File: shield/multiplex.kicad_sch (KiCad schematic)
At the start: 2 parts

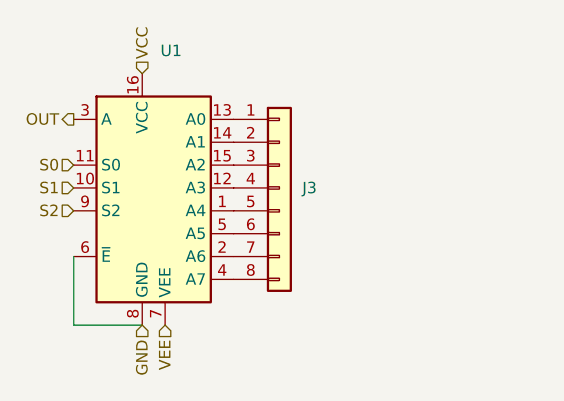
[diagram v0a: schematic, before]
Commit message: Move incomplete shield to separate dir, and add complete breakout design for a single multiplexer.
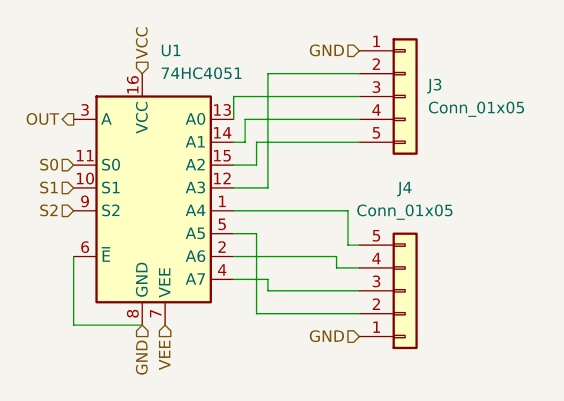
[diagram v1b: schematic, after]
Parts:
- removed J3: (no value), Connector_PinHeader_2.54mm:PinHeader_1x08_P2.54mm_Vertical, symbol Connector_Generic:Conn_01x08
- added J3, J4: Conn_01x05, Connector_PinHeader_2.54mm:PinHeader_1x05_P2.54mm_Vertical, symbol Connector_Generic:Conn_01x05
- U1: value (none) -> 74HC4051
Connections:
- net GND: now also J3.1 (Pin_1), J4.1 (Pin_1)
- net at U1.1 (A4): now also J4.5 (Pin_5)
- net at U1.12 (A3): now also J3.2 (Pin_2)
- net at U1.13 (A0): now also J3.3 (Pin_3)
- net at U1.14 (A1): now also J3.4 (Pin_4)
- net at U1.15 (A2): now also J3.5 (Pin_5)
- net at U1.2 (A6): now also J4.4 (Pin_4)
- net at U1.4 (A7): now also J4.3 (Pin_3)
- net at U1.5 (A5): now also J4.2 (Pin_2)
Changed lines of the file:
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@@
 (kicad_sch (version 20211123) (generator eeschema)
   (paper "A4")
+  (wire (pts (xy 104.14 49.53) (xy 104.14 62.23))
+    (stroke (width 0) (type default) (color 0 0 0 0))
+  )
+  (wire (pts (xy 100.33 72.39) (xy 104.14 72.39))
+    (stroke (width 0) (type default) (color 0 0 0 0))
+  )
   (wire (pts (xy 82.55 77.47) (xy 90.17 77.47))
     (stroke (width 0) (type default) (color 0 0 0 0))
   )
+  (wire (pts (xy 101.6 54.61) (xy 114.3 54.61))
+    (stroke (width 0) (type default) (color 0 0 0 0))
+  )
+  (wire (pts (xy 101.6 57.15) (xy 101.6 54.61))
+    (stroke (width 0) (type default) (color 0 0 0 0))
+  )
+  (wire (pts (xy 104.14 49.53) (xy 114.3 49.53))
+    (stroke (width 0) (type default) (color 0 0 0 0))
+  )
+  (wire (pts (xy 100.33 62.23) (xy 104.14 62.23))
+    (stroke (width 0) (type default) (color 0 0 0 0))
+  )
+  (wire (pts (xy 100.33 64.77) (xy 113.03 64.77))
+    (stroke (width 0) (type default) (color 0 0 0 0))
+  )
+  (wire (pts (xy 100.33 69.85) (xy 111.76 69.85))
+    (stroke (width 0) (type default) (color 0 0 0 0))
+  )
+  (wire (pts (xy 111.76 71.12) (xy 114.3 71.12))
+    (stroke (width 0) (type default) (color 0 0 0 0))
+  )
+  (wire (pts (xy 102.87 59.69) (xy 102.87 57.15))
+    (stroke (width 0) (type default) (color 0 0 0 0))
+  )
+  (wire (pts (xy 104.14 72.39) (xy 104.14 73.66))
+    (stroke (width 0) (type default) (color 0 0 0 0))
+  )
+  (wire (pts (xy 100.33 54.61) (xy 100.33 52.07))
+    (stroke (width 0) (type default) (color 0 0 0 0))
+  )
+  (wire (pts (xy 111.76 69.85) (xy 111.76 71.12))
+    (stroke (width 0) (type default) (color 0 0 0 0))
+  )
+  (wire (pts (xy 100.33 59.69) (xy 102.87 59.69))
+    (stroke (width 0) (type default) (color 0 0 0 0))
+  )
+  (wire (pts (xy 113.03 68.58) (xy 114.3 68.58))
+    (stroke (width 0) (type default) (color 0 0 0 0))
+  )
+  (wire (pts (xy 102.87 76.2) (xy 114.3 76.2))
+    (stroke (width 0) (type default) (color 0 0 0 0))
+  )
+  (wire (pts (xy 100.33 67.31) (xy 102.87 67.31))
+    (stroke (width 0) (type default) (color 0 0 0 0))
+  )
+  (wire (pts (xy 102.87 67.31) (xy 102.87 76.2))
+    (stroke (width 0) (type default) (color 0 0 0 0))
+  )
+  (wire (pts (xy 113.03 64.77) (xy 113.03 68.58))
+    (stroke (width 0) (type default) (color 0 0 0 0))
+  )
+  (wire (pts (xy 100.33 52.07) (xy 114.3 52.07))
+    (stroke (width 0) (type default) (color 0 0 0 0))
+  )
+  (wire (pts (xy 102.87 57.15) (xy 114.3 57.15))
+    (stroke (width 0) (type default) (color 0 0 0 0))
+  )
   (wire (pts (xy 82.55 69.85) (xy 82.55 77.47))
+    (stroke (width 0) (type default) (color 0 0 0 0))
+  )
+  (wire (pts (xy 104.14 73.66) (xy 114.3 73.66))
+    (stroke (width 0) (type default) (color 0 0 0 0))
+  )
+  (wire (pts (xy 100.33 57.15) (xy 101.6 57.15))
     (stroke (width 0) (type default) (color 0 0 0 0))
   )
@@
     (effects (font (size 1.27 1.27)) (justify left))
   )
+  (hierarchical_label "GND" (shape input) (at 114.3 46.99 180)
+    (effects (font (size 1.27 1.27)) (justify right))
+  )
   (hierarchical_label "GND" (shape input) (at 90.17 77.47 270)
+    (effects (font (size 1.27 1.27)) (justify right))
+  )
+  (hierarchical_label "GND" (shape input) (at 114.3 78.74 180)
     (effects (font (size 1.27 1.27)) (justify right))
   )
@@
     (effects (font (size 1.27 1.27)) (justify right))
   )
+  (symbol (lib_id "Connector_Generic:Conn_01x05") (at 119.38 52.07 0) (unit 1)
+    (in_bom yes) (on_board yes) (fields_autoplaced)
+    (property "Reference" "J3" (id 0) (at 121.92 50.7999 0)
+      (effects (font (size 1.27 1.27)) (justify left))
+    )
+    (property "Value" "Conn_01x05" (id 1) (at 121.92 53.3399 0)
+      (effects (font (size 1.27 1.27)) (justify left))
+    )
+    (property "Footprint" "Connector_PinHeader_2.54mm:PinHeader_1x05_P2.54mm_Vertical" (id 2) (at 119.38 52.07 0)
+      (effects (font (size 1.27 1.27)) hide)
+    )
+    (property "Datasheet" "~" (id 3) (at 119.38 52.07 0)
+      (effects (font (size 1.27 1.27)) hide)
+    )
+    (pin "1")
+    (pin "2")
+    (pin "3")
+    (pin "4")
+    (pin "5")
+  )
+  (symbol (lib_id "Connector_Generic:Conn_01x05") (at 119.38 73.66 0) (mirror x) (unit 1)
+    (in_bom yes) (on_board yes) (fields_autoplaced)
+    (property "Reference" "J4" (id 0) (at 119.38 62.23 0))
+    (property "Value" "Conn_01x05" (id 1) (at 119.38 64.77 0))
+    (property "Footprint" "Connector_PinHeader_2.54mm:PinHeader_1x05_P2.54mm_Vertical" (id 2) (at 119.38 73.66 0)
+      (effects (font (size 1.27 1.27)) hide)
+    )
+    (property "Datasheet" "~" (id 3) (at 119.38 73.66 0)
+      (effects (font (size 1.27 1.27)) hide)
+    )
+    (pin "1")
+    (pin "2")
+    (pin "3")
+    (pin "4")
+    (pin "5")
+  )
   (symbol (lib_id "74xx:74HC4051") (at 90.17 62.23 0) (unit 1)
     (in_bom yes) (on_board yes) (fields_autoplaced)
@@
       (effects (font (size 1.27 1.27)) (justify left))
     )
-    (property "Value" "" (id 1) (at 92.1894 49.53 0)
+    (property "Value" "74HC4051" (id 1) (at 92.1894 49.53 0)
       (effects (font (size 1.27 1.27)) (justify left))
     )
@@
     (pin "9")
   )
-  (symbol (lib_id "Connector_Generic:Conn_01x08") (at 105.41 62.23 0) (unit 1)
-    (in_bom yes) (on_board yes) (fields_autoplaced)
-    (property "Reference" "J3" (id 0) (at 107.95 62.2299 0)
-      (effects (font (size 1.27 1.27)) (justify left))
-    )
-    (property "Value" "" (id 1) (at 107.95 64.7699 0)
-      (effects (font (size 1.27 1.27)) (justify left))
-    )
-    (property "Footprint" "Connector_PinHeader_2.54mm:PinHeader_1x08_P2.54mm_Vertical" (id 2) (at 105.41 62.23 0)
-      (effects (font (size 1.27 1.27)) hide)
-    )
-    (property "Datasheet" "~" (id 3) (at 105.41 62.23 0)
-      (effects (font (size 1.27 1.27)) hide)
-    )
-    (pin "1")
-    (pin "2")
-    (pin "3")
-    (pin "4")
-    (pin "5")
-    (pin "6")
-    (pin "7")
-    (pin "8")
-  )
 )
